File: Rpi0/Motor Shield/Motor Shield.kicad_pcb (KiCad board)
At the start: 2 copper layers, 29.8 x 64.8 mm, 30 parts, among them J1 Screw_Terminal_01x02, J2 Conn_02x01, J3 Conn_02x01, J4 Screw_Terminal_01x02, J5 Screw_Terminal_01x02, J6 Conn_01x04_Female, J7 Conn_01x04_Female, Q1 Q_PMOS_GDSD, U1 IFX9201SG, U2 IFX9201SG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

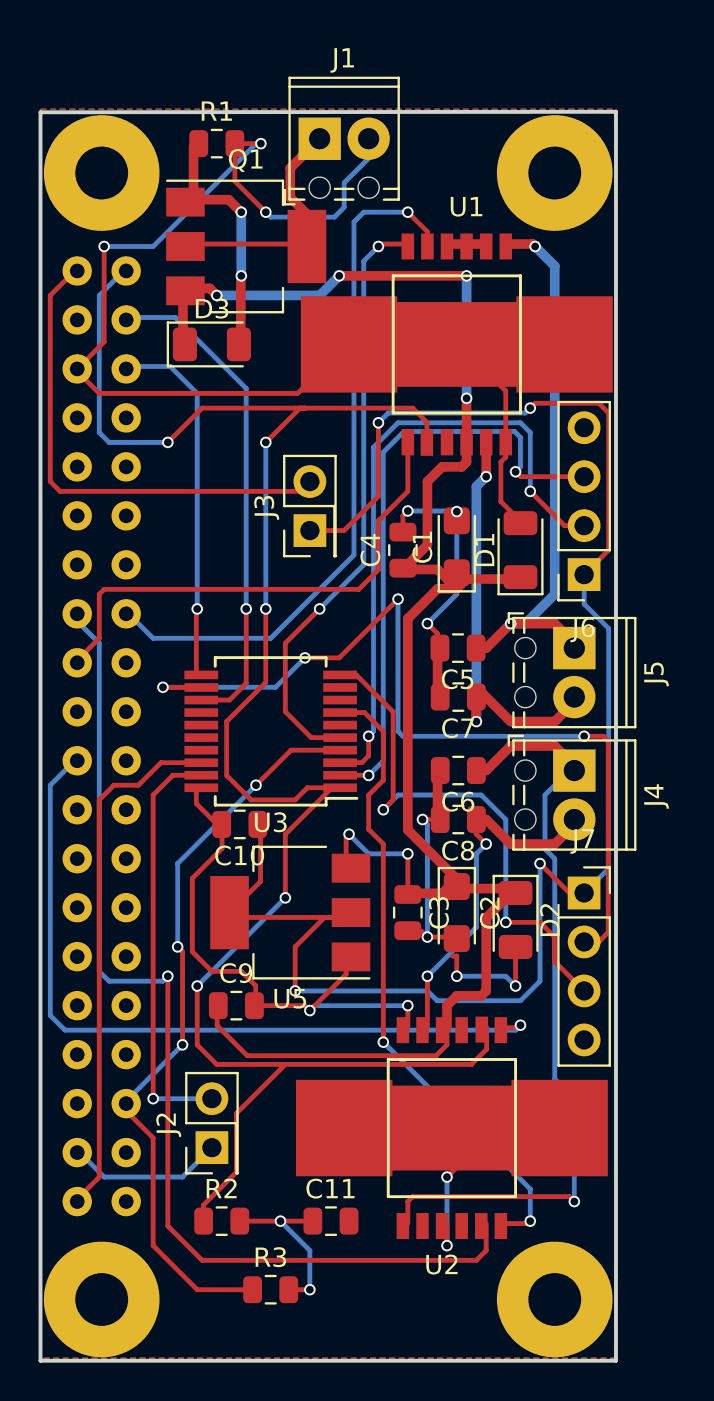
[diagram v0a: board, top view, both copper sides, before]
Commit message: Modified components compared to Mouser electronics stocks
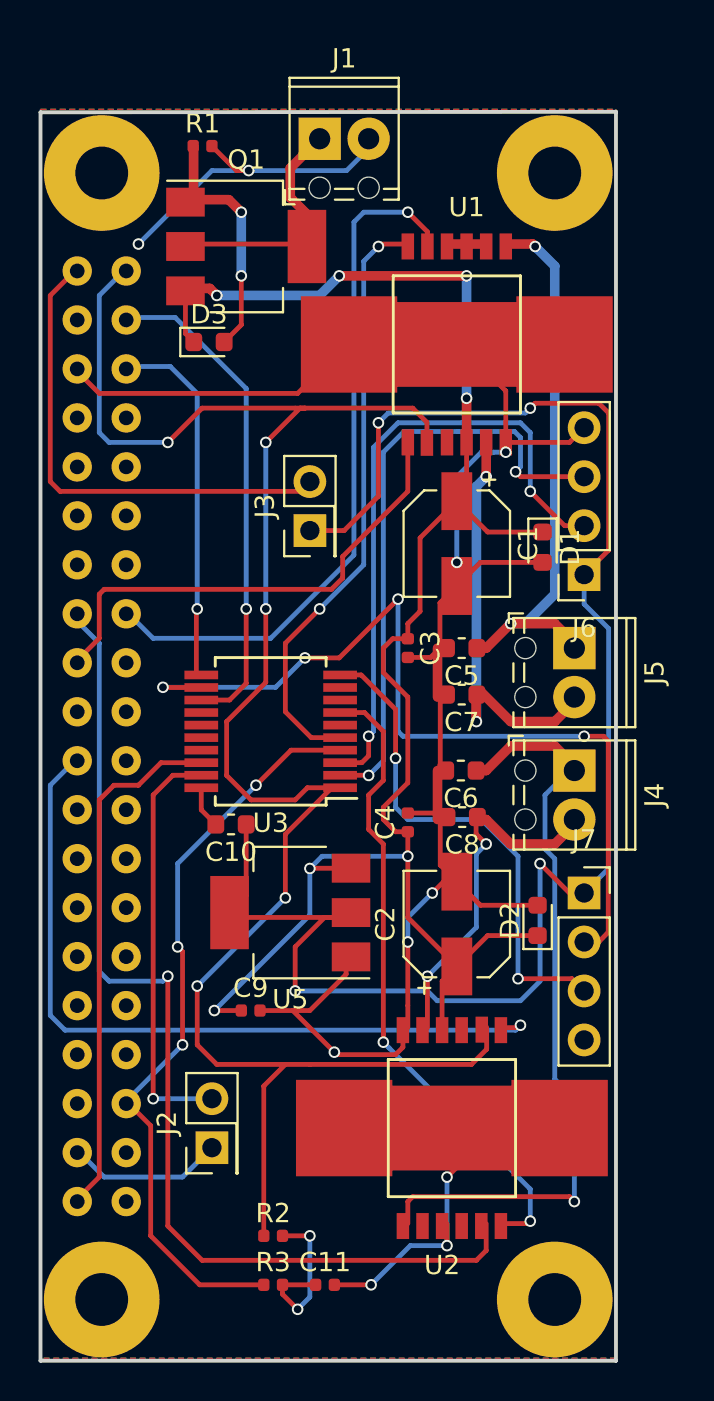
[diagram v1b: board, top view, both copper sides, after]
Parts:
- C1, C2: footprint Capacitor_Tantalum_SMD:CP_EIA-3216-18_Kemet-A -> Capacitor_SMD:CP_Elec_5x5.3
- C10, C5, C6, C7, C8: footprint Capacitor_SMD:C_0805_2012Metric -> Capacitor_SMD:C_0603_1608Metric
- C11, C3, C4, C9: footprint Capacitor_SMD:C_0805_2012Metric -> Capacitor_SMD:C_0402_1005Metric
- D1, D2, D3: footprint Diode_SMD:D_1206_3216Metric -> Diode_SMD:D_0603_1608Metric
- R1, R2, R3: footprint Resistor_SMD:R_0805_2012Metric -> Resistor_SMD:R_0402_1005Metric
- moved C4 14.1 mm to (161.3, 106.8)
- moved C3 13.7 mm to (161.3, 97.8)
- moved C11 3.32 mm to (157.0, 130.8)
- moved R2 2.77 mm to (154.3, 128.3)
- moved D1 1.15 mm to (168.3, 92.6), turned to 270 degrees
- moved D2 1.14 mm to (168.0, 111.9), turned to 90 degrees
- moved C9 0.78 mm to (153.1, 116.6)
- moved R1 0.75 mm to (150.6, 71.8)
- moved C2 0.59 mm to (163.8, 112.1), turned to 90 degrees
- moved C10 0.46 mm to (152.1, 106.9)
- moved R3 0.28 mm to (154.3, 130.8)
- moved C8 0.24 mm to (164.1, 106.6)
- moved C7 0.22 mm to (164.1, 100.2)
- moved D3 0.20 mm to (151.0, 81.9)
- moved C5 0.19 mm to (164.1, 97.8)
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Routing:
- net BAT-PROT+: track 97.4 -> 90.7 mm, vias 6 -> 7
- net BAT-: track 127.9 -> 123.6 mm, vias 14 -> 10
- net B2: track 27.9 -> 26.1 mm
- net +5V: track 87.2 -> 86.3 mm
- net DIR1: track 26.3 -> 25.4 mm
- net +3V3: track 98.8 -> 98.2 mm

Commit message: Missing connections
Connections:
- U1 pad 8: Net-(U1-Pad8) -> BAT-
- U1 pad 9: Net-(U1-Pad9) -> BAT-
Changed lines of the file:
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@@
     (zones 0)
     (modules 30)
-    (nets 68)
+    (nets 66)
   )
   (page A4)
@@
       (padsonsilk false)
       (subtractmaskfromsilk false)
-      (outputformat 1)
+      (outputformat 4)
       (mirror false)
       (drillshape 0)
       (scaleselection 1)
-      (outputdirectory "Gerber/"))
+      (outputdirectory "PDF/"))
   )
   (net 0 "")
@@
   (net 64 "Net-(J2-Pad2)")
   (net 65 "Net-(J3-Pad2)")
-  (net 66 "Net-(U1-Pad8)")
-  (net 67 "Net-(U1-Pad9)")
   (net_class Default "This is the default net class."
     (clearance 0.2)
@@
     (add_net "Net-(J2-Pad2)")
     (add_net "Net-(J3-Pad2)")
-    (add_net "Net-(U1-Pad8)")
-    (add_net "Net-(U1-Pad9)")
     (add_net "Net-(U3-Pad14)")
     (add_net "Net-(U3-Pad15)")
@@
       (net 3 OUT2))
     (pad 8 smd rect (at 1.524 -5.08) (size 0.65 1.35) (layers F.Cu F.Paste F.Mask)
-      (net 66 "Net-(U1-Pad8)"))
+      (net 2 BAT-))
     (pad 9 smd rect (at 0.508 -5.08) (size 0.65 1.35) (layers F.Cu F.Paste F.Mask)
-      (net 67 "Net-(U1-Pad9)"))
+      (net 2 BAT-))
     (pad 10 smd rect (at -0.508 -5.08) (size 0.65 1.35) (layers F.Cu F.Paste F.Mask)
       (net 2 BAT-))

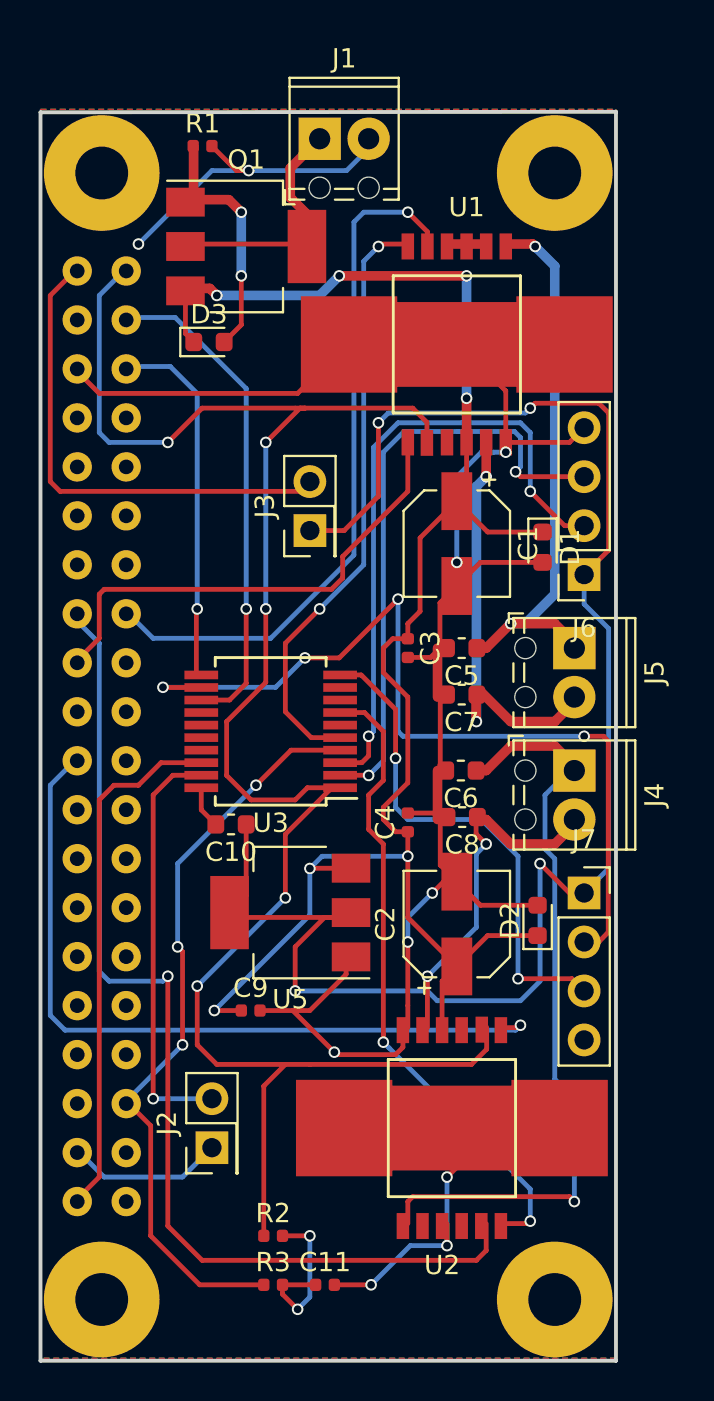
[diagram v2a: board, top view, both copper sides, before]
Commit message: Updated IFX9201 footprint for thermal pads
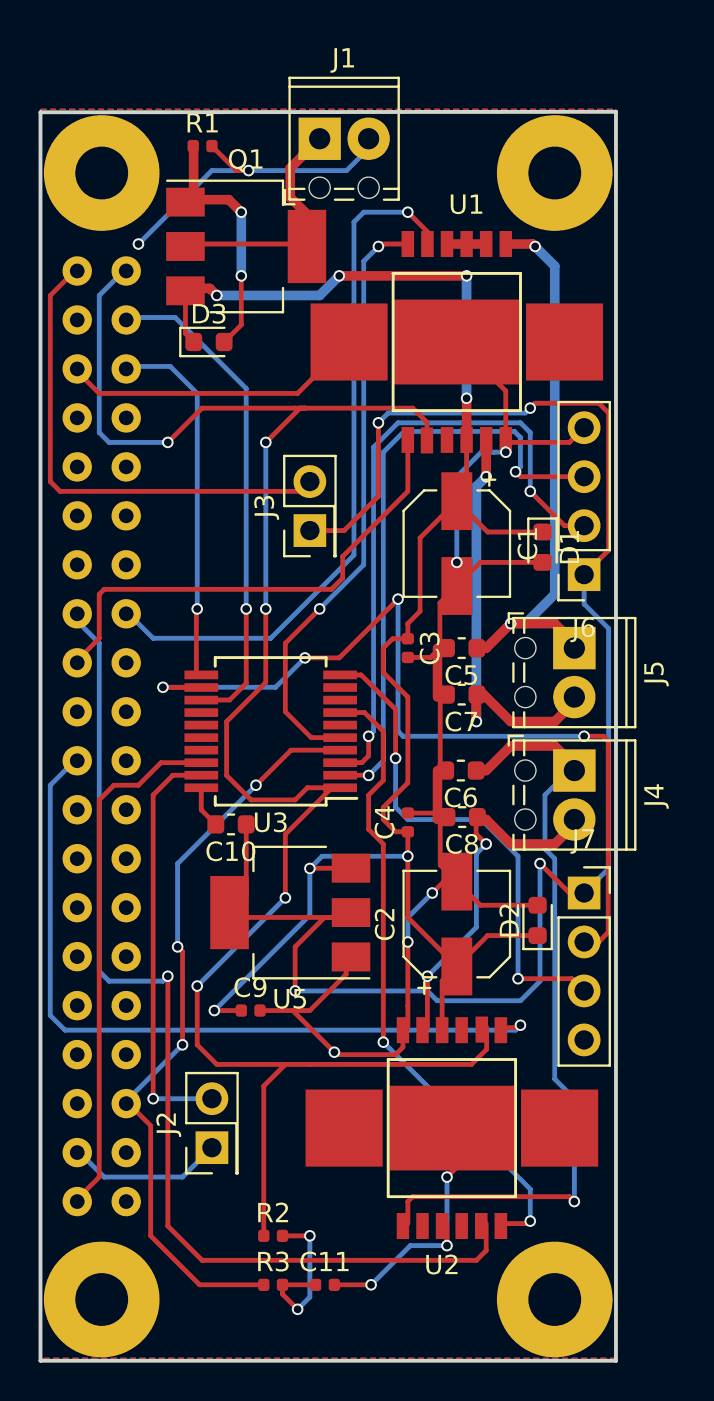
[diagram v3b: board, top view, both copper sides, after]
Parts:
- moved U1 0.13 mm to (163.8, 81.9)
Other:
- rule pad_to_mask_clearance: 0.2 -> 0.1
